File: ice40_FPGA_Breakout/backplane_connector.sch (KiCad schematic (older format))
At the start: 51 parts

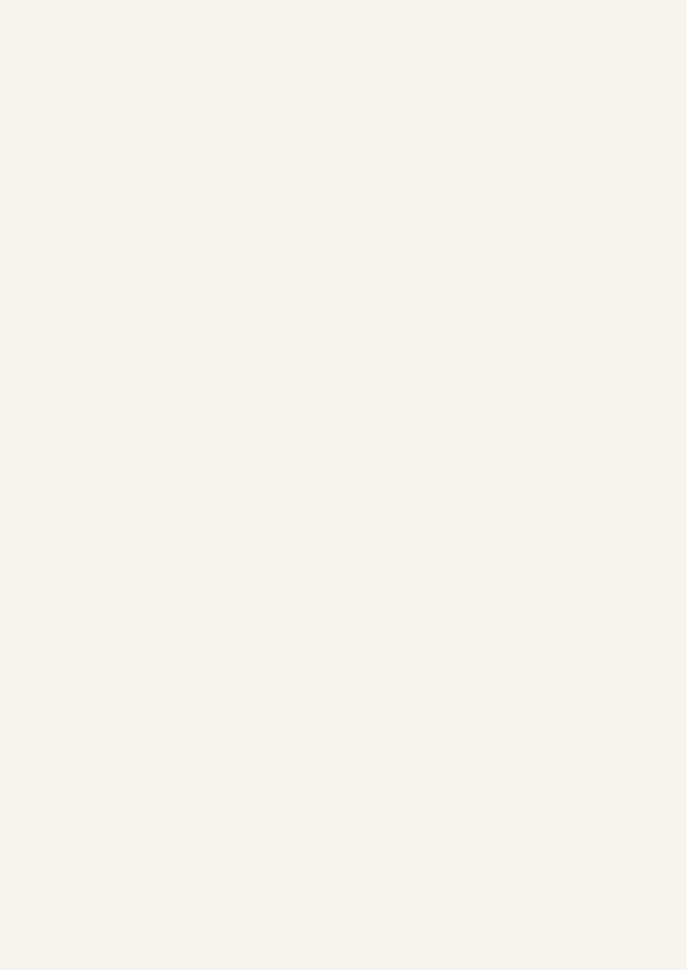
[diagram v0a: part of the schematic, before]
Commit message: mother board to backplane connector added, power connector added
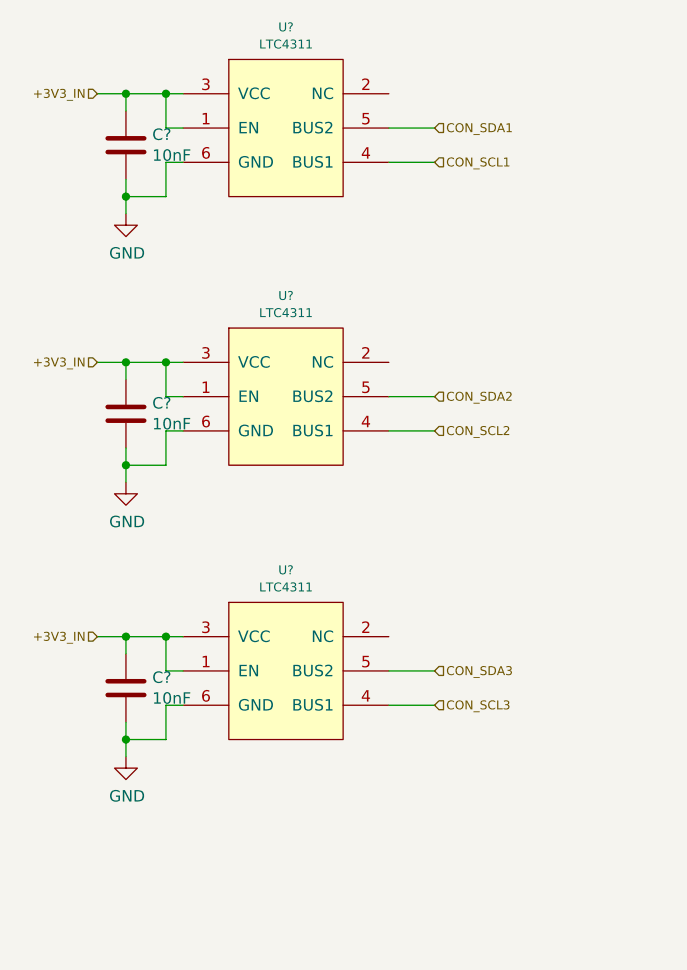
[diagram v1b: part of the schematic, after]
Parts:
- added C? (x3): 10nF, Capacitor_SMD:C_0402_1005Metric, symbol device:C
- added U? (x3): LTC4311, Package_DFN_QFN:DFN-6-1EP_2x2mm_P0.5mm_EP0.61x1.42mm, symbol gti_Lattice:LTC4311
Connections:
- net labels added: +3V3_IN, CON_SCL1, CON_SCL2, CON_SCL3, CON_SDA1, CON_SDA2, CON_SDA3, GND
- wire segments 170 -> 209
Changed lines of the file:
@@
 $Descr A4 11693 8268
 encoding utf-8
-Sheet 3 5
+Sheet 3 6
 Title ""
 Date ""
@@
 Text Notes 1300 675  0    60   ~ 0
 Differential Signals/Clock\n
+$Comp
+L gti_Lattice:LTC4311 U?
+U 1 1 5D11931D
+P -2625 225
+F 0 "U?" H -2625 366 39  0000 C CNN
+F 1 "LTC4311" H -2625 291 39  0000 C CNN
+F 2 "Package_DFN_QFN:DFN-6-1EP_2x2mm_P0.5mm_EP0.61x1.42mm" H -2625 225 39  0001 C CNN
+F 3 "" H -2625 225 39  0001 C CNN
+	1    -2625 225
+	1    0    0    -1
+$EndComp
+Text HLabel -3450 375  0    39   Input ~ 0
++3V3_IN
+Wire Wire Line
+	-3450 375  -3325 375
+Wire Wire Line
+	-3075 525  -3150 525
+Wire Wire Line
+	-3150 525  -3150 375
+Connection ~ -3150 375
+Wire Wire Line
+	-3150 375  -3075 375
+$Comp
+L device:C C?
+U 1 1 5D1633D6
+P -3325 600
+F 0 "C?" H -3210 646 50  0000 L CNN
+F 1 "10nF" H -3210 555 50  0000 L CNN
+F 2 "Capacitor_SMD:C_0402_1005Metric" H -3287 450 50  0001 C CNN
+F 3 "" H -3325 600 50  0001 C CNN
+	1    -3325 600
+	1    0    0    -1
+$EndComp
+Wire Wire Line
+	-3325 450  -3325 375
+Connection ~ -3325 375
+Wire Wire Line
+	-3325 375  -3150 375
+Wire Wire Line
+	-3325 750  -3325 825
+Wire Wire Line
+	-3325 825  -3150 825
+Wire Wire Line
+	-3150 825  -3150 675
+Wire Wire Line
+	-3150 675  -3075 675
+$Comp
+L power:GND #PWR?
+U 1 1 5D198CFB
+P -3325 900
+F 0 "#PWR?" H -3325 650 50  0001 C CNN
+F 1 "GND" H -3320 727 50  0000 C CNN
+F 2 "" H -3325 900 50  0001 C CNN
+F 3 "" H -3325 900 50  0001 C CNN
+	1    -3325 900
+	1    0    0    -1
+$EndComp
+Wire Wire Line
+	-3325 900  -3325 825
+Connection ~ -3325 825
+Wire Wire Line
+	-2175 525  -1975 525
+Wire Wire Line
+	-2175 675  -1975 675
+Text HLabel -1975 525  2    39   Input ~ 0
+CON_SDA1
+Text HLabel -1975 675  2    39   Input ~ 0
+CON_SCL1
+$Comp
+L gti_Lattice:LTC4311 U?
+U 1 1 5D1C0206
+P -2625 1400
+F 0 "U?" H -2625 1541 39  0000 C CNN
+F 1 "LTC4311" H -2625 1466 39  0000 C CNN
+F 2 "Package_DFN_QFN:DFN-6-1EP_2x2mm_P0.5mm_EP0.61x1.42mm" H -2625 1400 39  0001 C CNN
+F 3 "" H -2625 1400 39  0001 C CNN
+	1    -2625 1400
+	1    0    0    -1
+$EndComp
+Text HLabel -3450 1550 0    39   Input ~ 0
++3V3_IN
+Wire Wire Line
+	-3450 1550 -3325 1550
+Wire Wire Line
+	-3075 1700 -3150 1700
+Wire Wire Line
+	-3150 1700 -3150 1550
+Connection ~ -3150 1550
+Wire Wire Line
+	-3150 1550 -3075 1550
+$Comp
+L device:C C?
+U 1 1 5D1C0213
+P -3325 1775
+F 0 "C?" H -3210 1821 50  0000 L CNN
+F 1 "10nF" H -3210 1730 50  0000 L CNN
+F 2 "Capacitor_SMD:C_0402_1005Metric" H -3287 1625 50  0001 C CNN
+F 3 "" H -3325 1775 50  0001 C CNN
+	1    -3325 1775
+	1    0    0    -1
+$EndComp
+Wire Wire Line
+	-3325 1625 -3325 1550
+Connection ~ -3325 1550
+Wire Wire Line
+	-3325 1550 -3150 1550
+Wire Wire Line
+	-3325 1925 -3325 2000
+Wire Wire Line
+	-3325 2000 -3150 2000
+Wire Wire Line
+	-3150 2000 -3150 1850
+Wire Wire Line
+	-3150 1850 -3075 1850
+$Comp
+L power:GND #PWR?
+U 1 1 5D1C0221
+P -3325 2075
+F 0 "#PWR?" H -3325 1825 50  0001 C CNN
+F 1 "GND" H -3320 1902 50  0000 C CNN
+F 2 "" H -3325 2075 50  0001 C CNN
+F 3 "" H -3325 2075 50  0001 C CNN
+	1    -3325 2075
+	1    0    0    -1
+$EndComp
+Wire Wire Line
+	-3325 2075 -3325 2000
+Connection ~ -3325 2000
+Wire Wire Line
+	-2175 1700 -1975 1700
+Wire Wire Line
+	-2175 1850 -1975 1850
+Text HLabel -1975 1700 2    39   Input ~ 0
+CON_SDA2
+Text HLabel -1975 1850 2    39   Input ~ 0
+CON_SCL2
+$Comp
+L gti_Lattice:LTC4311 U?
+U 1 1 5D1CF416
+P -2625 2600
+F 0 "U?" H -2625 2741 39  0000 C CNN
+F 1 "LTC4311" H -2625 2666 39  0000 C CNN
+F 2 "Package_DFN_QFN:DFN-6-1EP_2x2mm_P0.5mm_EP0.61x1.42mm" H -2625 2600 39  0001 C CNN
+F 3 "" H -2625 2600 39  0001 C CNN
+	1    -2625 2600
+	1    0    0    -1
+$EndComp
+Text HLabel -3450 2750 0    39   Input ~ 0
++3V3_IN
+Wire Wire Line
+	-3450 2750 -3325 2750
+Wire Wire Line
+	-3075 2900 -3150 2900
+Wire Wire Line
+	-3150 2900 -3150 2750
+Connection ~ -3150 2750
+Wire Wire Line
+	-3150 2750 -3075 2750
+$Comp
+L device:C C?
+U 1 1 5D1CF423
+P -3325 2975
+F 0 "C?" H -3210 3021 50  0000 L CNN
+F 1 "10nF" H -3210 2930 50  0000 L CNN
+F 2 "Capacitor_SMD:C_0402_1005Metric" H -3287 2825 50  0001 C CNN
+F 3 "" H -3325 2975 50  0001 C CNN
+	1    -3325 2975
+	1    0    0    -1
+$EndComp
+Wire Wire Line
+	-3325 2825 -3325 2750
+Connection ~ -3325 2750
+Wire Wire Line
+	-3325 2750 -3150 2750
+Wire Wire Line
+	-3325 3125 -3325 3200
+Wire Wire Line
+	-3325 3200 -3150 3200
+Wire Wire Line
+	-3150 3200 -3150 3050
+Wire Wire Line
+	-3150 3050 -3075 3050
+$Comp
+L power:GND #PWR?
+U 1 1 5D1CF431
+P -3325 3275
+F 0 "#PWR?" H -3325 3025 50  0001 C CNN
+F 1 "GND" H -3320 3102 50  0000 C CNN
+F 2 "" H -3325 3275 50  0001 C CNN
+F 3 "" H -3325 3275 50  0001 C CNN
+	1    -3325 3275
+	1    0    0    -1
+$EndComp
+Wire Wire Line
+	-3325 3275 -3325 3200
+Connection ~ -3325 3200
+Wire Wire Line
+	-2175 2900 -1975 2900
+Wire Wire Line
+	-2175 3050 -1975 3050
+Text HLabel -1975 2900 2    39   Input ~ 0
+CON_SDA3
+Text HLabel -1975 3050 2    39   Input ~ 0
+CON_SCL3
 $EndSCHEMATC
